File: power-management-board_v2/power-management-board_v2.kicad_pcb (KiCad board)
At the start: 2 copper layers, 90 x 70 mm, 130 parts, among them IC2 TLP7820_TP4,E, IC3 MCP2562, J1 Conn_01x02, J2 Conn_01x02, J3 Conn_01x04, J4 Conn_01x04, J5 Conn_01x04_Pin, J6 Conn_01x02_Pin, J7 Conn_01x02, J8 Conn_01x02, J9 Conn_01x02, Q3 SSM3K341R, Q4 SSM3K341R, SW1 SW_Push, SW3 SW_SPDT_312, U1 TLP293, U2 TPS54560BDDA, U3 STM32G431K8Tx, U4 NJM12888F33, U5 TLP293, U6 CZ3A07, U7 AP7375, U8 TLP293

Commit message: 完成
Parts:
- added D10: SS2040FL, 0Ikedalibrary:SOD-123FL, F.Cu at (42.1, 39.1)
- added D8: LED, LED_SMD:LED_0603_1608Metric_Pad1.05x0.95mm_HandSolder, F.Cu at (104.0, 24.3)
- added JP1: Jumper_2_Open, Connector_PinHeader_2.54mm:PinHeader_1x02_P2.54mm_Vertical, F.Cu at (33.7, 31.4)
- added K1: FBR562ND12-W, 0Ikedalibrary:FBR562ND12-W, F.Cu at (34.2, 53.7)
- added R34: 10k, Resistor_SMD:R_0603_1608Metric_Pad0.98x0.95mm_HandSolder, F.Cu at (37.5, 39.5)
- added R40: 10k, Resistor_SMD:R_0603_1608Metric_Pad0.98x0.95mm_HandSolder, B.Cu at (45.2, 34.5)
- added R41: 10k, Resistor_SMD:R_0603_1608Metric_Pad0.98x0.95mm_HandSolder, F.Cu at (101.5, 23.4)
- added U9: TLP293, Package_SO:SOIC-4_4.55x2.6mm_P1.27mm, B.Cu at (44.7, 39.6)
- C2, C27, D29, D30, Q3, Q4, R11, R12, R13, R14, R26, R30, R47: moved to B.Cu
- moved C29 148.3 mm to (100.5, 25.1)
- moved R2 141.3 mm to (94.2, 33.7), turned to -90 degrees
- moved R1 141.0 mm to (92.6, 26.3), turned to -90 degrees
- moved R7 139.2 mm to (96.4, 23.7), turned to 180 degrees
- moved C28 138.6 mm to (93.3, 36.2), turned to 180 degrees
- moved C26 137.8 mm to (92.6, 33.7), turned to -90 degrees
- moved R8 136.5 mm to (93.0, 23.7), turned to 180 degrees
- moved R29 135.9 mm to (92.6, 29.9), turned to 90 degrees
- moved R28 133.3 mm to (91.0, 31.7), turned to 90 degrees
- moved C30 130.5 mm to (101.1, 43.5), turned to -90 degrees
- moved C31 127.4 mm to (97.7, 43.5), turned to -90 degrees
- moved C25 125.9 mm to (93.9, 21.2), turned to 180 degrees
- moved C24 125.7 mm to (93.9, 17.8), turned to 180 degrees
- moved L1 122.3 mm to (99.4, 36.6), turned to -90 degrees
- moved D1 111.6 mm to (100.7, 29.1), turned to 90 degrees
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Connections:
- C2 pad 2: GND -> GNDPWR
- C27 pad 2: GND -> GNDPWR
- U3 pad 28: unconnected-(U3-PB5-Pad28) -> VCC_check
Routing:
- net +12VA: track 0.00 -> 69.7 mm, vias 0 -> 2
- net EN_return: track 0.00 -> 42.2 mm
- net stm32_EN_2: track 0.00 -> 40.2 mm, vias 0 -> 4
- net GND: track 21.4 -> 60.2 mm, vias 148 -> 86
- net stm32_EN_1: track 0.00 -> 38.7 mm, vias 0 -> 4
- net Net-(D29-A): track 0.00 -> 35.8 mm
- net VCC: track 0.00 -> 24.0 mm
- net Net-(K1B-N.C.): track 0.00 -> 22.7 mm
- net Net-(K1A-COM): track 0.00 -> 21.9 mm
- net +12V: track 15.6 -> 36.8 mm
- net VOUT: track 19.4 -> 0.00 mm, vias 87 -> 71
- net Net-(K1A-N.C.): track 0.00 -> 19.4 mm, vias 0 -> 1
- net INPUT_relay: track 8.15 -> 26.7 mm, vias 68 -> 55
- net VCC_check: track 0.00 -> 18.0 mm, vias 0 -> 1
- net Net-(D30-A): track 0.00 -> 17.1 mm
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- added copper zone on F.Cu, net +12V
- added copper zone on B.Cu, net GNDPWR
- added copper zone on F.Cu, net GNDPWR
- added copper zone on F.Cu, net Net-(D1-K)
- removed copper zone on B.Cu, net (none)
- removed copper zone on F.Cu, net (none)
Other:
- board text added: "12V"
- board text added: "12V OUT"
- board text added: "12V生成 入力"
- board text added: "EMS"
- board text removed: "2 1 G"
- board text removed: "EMS OUT"
- board text removed: "FAULT"
- board text removed: "IN1"
- board text removed: "IN2"
- board text removed: "i"
- board text removed: "s"
- board text removed: "逆接"

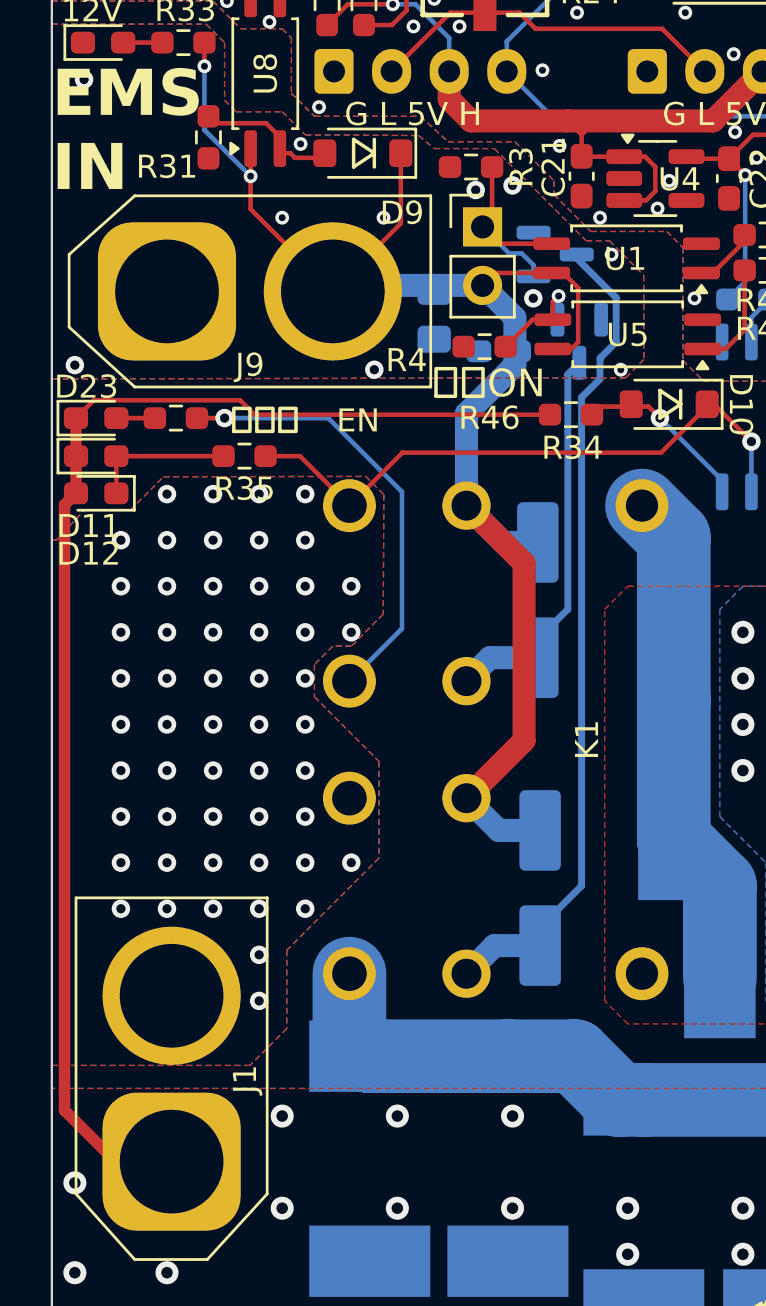
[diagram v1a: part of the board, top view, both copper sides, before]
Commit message: feat:ゲートに抵抗追加＆常時ON削除
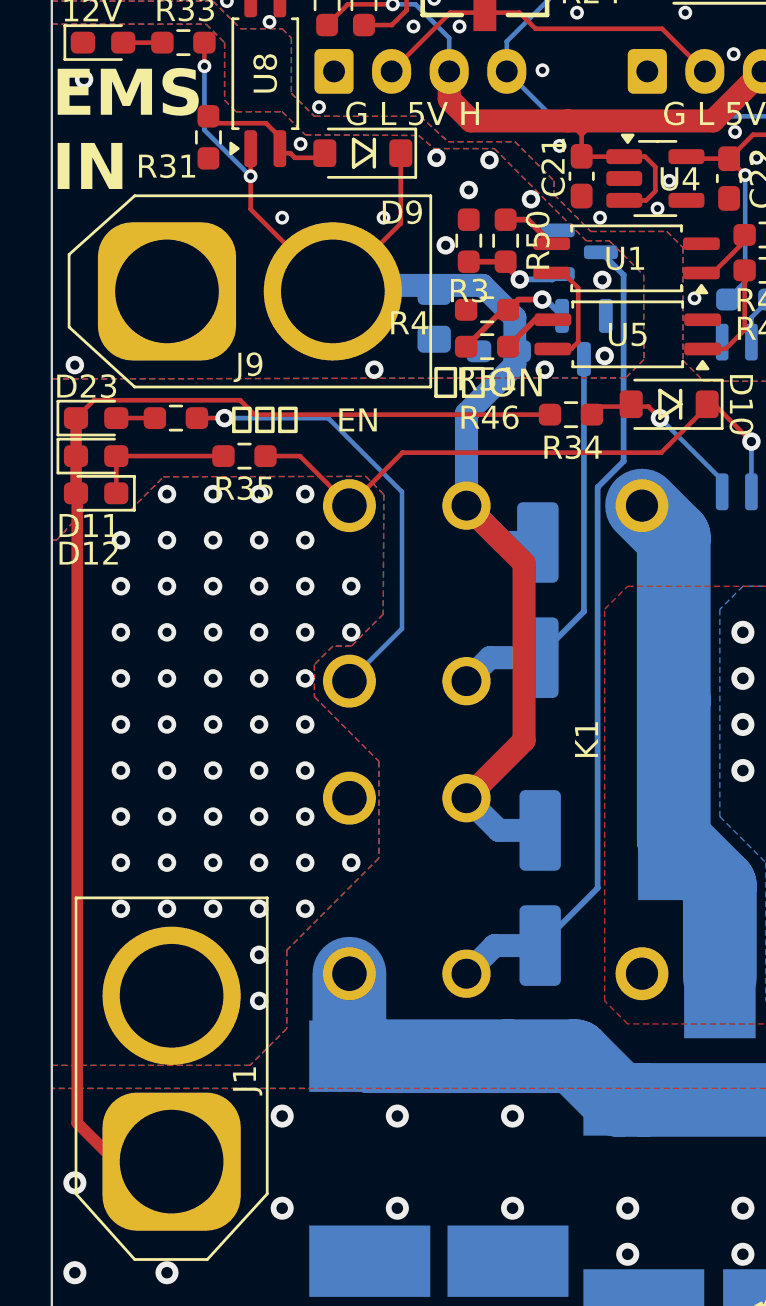
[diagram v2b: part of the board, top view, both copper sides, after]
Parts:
- removed JP1: Jumper_2_Open, Connector_PinHeader_2.54mm:PinHeader_1x02_P2.54mm_Vertical
- added R50: 470, Resistor_SMD:R_0603_1608Metric_Pad0.98x0.95mm_HandSolder, F.Cu at (34.7, 32.0)
- added R51: 470, Resistor_SMD:R_0603_1608Metric_Pad0.98x0.95mm_HandSolder, F.Cu at (33.9, 36.6)
- moved R3 3.20 mm to (33.1, 32.0), turned to 90 degrees
- moved R4 1.60 mm to (33.9, 35.0)
- moved Q3 1.05 mm to (37.9, 32.5)
- moved Q4 0.26 mm to (38.1, 36.2)
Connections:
- Q3 pad 1: GATE_A -> Net-(Q3-G)
- Q4 pad 1: GATE_B -> Net-(Q4-G)
- R3 pad 1: GATE_A -> Net-(Q3-G)
- R4 pad 1: GATE_B -> Net-(Q4-G)
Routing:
- net GATE_A: track 9.75 -> 2.43 mm
- net Net-(Q4-G): track 0.00 -> 5.30 mm, vias 0 -> 1
- net Net-(Q3-G): track 0.00 -> 4.37 mm, vias 0 -> 1
- net +12VA: track 69.7 -> 66.5 mm
- net GATE_B: track 4.71 -> 2.42 mm, vias 1 -> 0
- net GNDPWR: vias 11 -> 14

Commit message: シルク調整、DRC通した
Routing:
- net +12VA: track 66.5 -> 68.0 mm, vias 2 -> 3
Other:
- board text added: "VIN 逆接"
- board text added: "ソフトスタートOK"
- board text removed: "常時ON"
- board text removed: "駆動系"
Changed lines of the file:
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@@
 		(tags "resistor handsolder")
 		(property "Reference" "R46"
-			(at -13.6125 0 0)
+			(at -2.9125 1.95 0)
 			(layer "F.SilkS")
 			(effects
@@
 		(tags "resistor handsolder")
 		(property "Reference" "R3"
-			(at -2.2 0 0)
+			(at 2.05 0 0)
 			(layer "F.SilkS")
 			(effects
@@
 		(tags "resistor handsolder")
 		(property "Reference" "R50"
-			(at 0 -1.43 90)
+			(at -2.85 0 90)
 			(layer "F.SilkS")
 			(effects
@@
 		(tags "resistor handsolder")
 		(property "Reference" "R35"
-			(at 0 -1.43 0)
+			(at -3.0875 0 0)
 			(layer "F.SilkS")
 			(effects
@@
 		(tags "resistor handsolder")
 		(property "Reference" "R51"
-			(at 0 -1.43 0)
+			(at 0 -2.4 0)
 			(layer "F.SilkS")
 			(effects
@@
 		(tags "XT60 female vertical")
 		(property "Reference" "J9"
-			(at 3.6 3.2 180)
+			(at 5.35 3.55 180)
 			(layer "F.SilkS")
 			(effects
@@
 		(tags "resistor handsolder")
 		(property "Reference" "R4"
-			(at 3.3875 -0.6 0)
+			(at -0.05 -2.8 0)
 			(layer "F.SilkS")
 			(effects
@@
 		(tags "SOT TO_SOT_SMD")
 		(property "Reference" "Q4"
-			(at -2.3625 -0.8 180)
+			(at 0 -2.9 180)
 			(layer "B.SilkS")
 			(effects
@@
 		(tags "SOT TO_SOT_SMD")
 		(property "Reference" "Q3"
-			(at 1.85 -1.1 0)
+			(at 2.85 0 0)
 			(layer "B.SilkS")
 			(effects
@@
 		)
 	)
-	(gr_text "駆動系"
-		(at 22.75 40.4 0)
+	(gr_text "VIN\n逆接"
+		(at 18.65 43.7 0)
 		(layer "F.SilkS")
 		(effects
@@
 		)
 	)
-	(gr_text "5V 3.3V"
-		(at 25 16.6 0)
+	(gr_text "ソフトスタートOK"
+		(at 21.95 40.35 0)
 		(layer "F.SilkS")
 		(effects
@@
 		)
 	)
-	(gr_text "EN"
-		(at 27.35 40.4 0)
+	(gr_text "5V 3.3V"
+		(at 25 16.6 0)
 		(layer "F.SilkS")
 		(effects
@@
 		)
 	)
-	(gr_text "常時ON"
-		(at 31.5 38.9 0)
-		(layer "F.SilkS")
-		(effects
-			(font
-				(size 1.2 1.2)
-				(thickness 0.1524)
-			)
-			(justify left bottom)
-		)
-	)
 	(gr_text "EMS\nIN"
 		(at 15 30 0)
@@
 	)
 	(segment
+		(start 36.75 36.7)
+		(end 35.9 36.7)
+		(width 0.25)
+		(layer "F.Cu")
+		(net "+12VA")
+	)
+	(segment
 		(start 23.63 28)
 		(end 23.63 30.63)
@@
 	)
 	(via
+		(at 35.9 36.7)
+		(size 0.8)
+		(drill 0.4)
+		(layers "F.Cu" "B.Cu")
+		(net "+12VA")
+	)
+	(via
 		(at 23.63 29.2)
 		(size 0.6)
@@
 	)
 	(segment
+		(start 35.3625 36.7)
+		(end 35.2625 36.8)
+		(width 0.25)
+		(layer "B.Cu")
+		(net "+12VA")
+	)
+	(segment
 		(start 34.6 45.1)
 		(end 36.1 45.1)
@@
 	)
 	(segment
+		(start 35.9 36.7)
+		(end 35.3625 36.7)
+		(width 0.25)
+		(layer "B.Cu")
+		(net "+12VA")
+	)
+	(segment
 		(start 33.7 33.96)
 		(end 33.68 33.94)
@@
 	)
 	(segment
-		(start 34.7 31.0875)
-		(end 35.6575 31.0875)
+		(start 34.7 32.9125)
+		(end 34.7 33.067457)
 		(width 0.25)
 		(layer "F.Cu")
-		(net "GATE_A")
+		(net "Net-(Q3-G)")
 	)
 	(segment
-		(start 35.6575 31.0875)
-		(end 36.7 32.13)
+		(start 34.7 33.067457)
+		(end 35.314233 33.68169)
 		(width 0.25)
 		(layer "F.Cu")
-		(net "GATE_A")
+		(net "Net-(Q3-G)")
+	)
+	(segment
+		(start 34.7 32.9125)
+		(end 33.1 32.9125)
+		(width 0.25)
+		(layer "F.Cu")
+		(net "Net-(Q3-G)")
+	)
+	(via
+		(at 35.314233 33.68169)
+		(size 0.8)
+		(drill 0.4)
+		(layers "F.Cu" "B.Cu")
+		(net "Net-(Q3-G)")
+	)
+	(segment
+		(start 36.73081 33.68169)
+		(end 36.9625 33.45)
+		(width 0.25)
+		(layer "B.Cu")
+		(net "Net-(Q3-G)")
+	)
+	(segment
+		(start 35.314233 33.68169)
+		(end 36.73081 33.68169)
+		(width 0.25)
+		(layer "B.Cu")
+		(net "Net-(Q3-G)")
 	)
 	(via
@@
 	)
 	(segment
+		(start 34.7 31.0875)
+		(end 35.6575 31.0875)
+		(width 0.25)
+		(layer "F.Cu")
+		(net "GATE_A")
+	)
+	(segment
+		(start 35.6575 31.0875)
+		(end 36.7 32.13)
+		(width 0.25)
+		(layer "F.Cu")
+		(net "GATE_A")
+	)
+	(segment
 		(start 79.6 51.7125)
 		(end 79.6 50)
@@
 	)
 	(segment
+		(start 35.2575 34.555)
+		(end 36.291055 34.555)
+		(width 0.25)
+		(layer "F.Cu")
+		(net "Net-(Q4-G)")
+	)
+	(segment
+		(start 34.5875 35)
+		(end 32.9875 36.6)
+		(width 0.25)
+		(layer "F.Cu")
+		(net "Net-(Q4-G)")
+	)
+	(segment
+		(start 34.8125 35)
+		(end 34.5875 35)
+		(width 0.25)
+		(layer "F.Cu")
+		(net "Net-(Q4-G)")
+	)
+	(segment
+		(start 34.8125 35)
+		(end 35.2575 34.555)
+		(width 0.25)
+		(layer "F.Cu")
+		(net "Net-(Q4-G)")
+	)
+	(via
+		(at 36.291055 34.555)
+		(size 0.8)
+		(drill 0.4)
+		(layers "F.Cu" "B.Cu")
+		(net "Net-(Q4-G)")
+	)
+	(segment
+		(start 36.291055 34.555)
+		(end 36.4425 34.555)
+		(width 0.25)
+		(layer "B.Cu")
+		(net "Net-(Q4-G)")
+	)
+	(segment
+		(start 36.4425 34.555)
+		(end 37.15 35.2625)
+		(width 0.25)
+		(layer "B.Cu")
+		(net "Net-(Q4-G)")
+	)
+	(segment
 		(start 76 19.0675)
 		(end 76 20.6375)
@@
 		(net "Net-(U2-BOOT)")
 	)
-	(segment
-		(start 34.7 32.9125)
-		(end 34.7 33.067457)
-		(width 0.25)
-		(layer "F.Cu")
-		(net "Net-(Q3-G)")
-	)
-	(segment
-		(start 34.7 33.067457)
-		(end 35.314233 33.68169)
-		(width 0.25)
-		(layer "F.Cu")
-		(net "Net-(Q3-G)")
-	)
-	(segment
-		(start 34.7 32.9125)
-		(end 33.1 32.9125)
-		(width 0.25)
-		(layer "F.Cu")
-		(net "Net-(Q3-G)")
-	)
-	(via
-		(at 35.314233 33.68169)
-		(size 0.8)
-		(drill 0.4)
-		(layers "F.Cu" "B.Cu")
-		(net "Net-(Q3-G)")
-	)
-	(segment
-		(start 36.73081 33.68169)
-		(end 36.9625 33.45)
-		(width 0.25)
-		(layer "B.Cu")
-		(net "Net-(Q3-G)")
-	)
-	(segment
-		(start 35.314233 33.68169)
-		(end 36.73081 33.68169)
-		(width 0.25)
-		(layer "B.Cu")
-		(net "Net-(Q3-G)")
-	)
-	(segment
-		(start 35.2575 34.555)
-		(end 36.291055 34.555)
-		(width 0.25)
-		(layer "F.Cu")
-		(net "Net-(Q4-G)")
-	)
-	(segment
-		(start 34.5875 35)
-		(end 32.9875 36.6)
-		(width 0.25)
-		(layer "F.Cu")
-		(net "Net-(Q4-G)")
-	)
-	(segment
-		(start 34.8125 35)
-		(end 34.5875 35)
-		(width 0.25)
-		(layer "F.Cu")
-		(net "Net-(Q4-G)")
-	)
-	(segment
-		(start 34.8125 35)
-		(end 35.2575 34.555)
-		(width 0.25)
-		(layer "F.Cu")
-		(net "Net-(Q4-G)")
-	)
-	(via
-		(at 36.291055 34.555)
-		(size 0.8)
-		(drill 0.4)
-		(layers "F.Cu" "B.Cu")
-		(net "Net-(Q4-G)")
-	)
-	(segment
-		(start 36.291055 34.555)
-		(end 36.4425 34.555)
-		(width 0.25)
-		(layer "B.Cu")
-		(net "Net-(Q4-G)")
-	)
-	(segment
-		(start 36.4425 34.555)
-		(end 37.15 35.2625)
-		(width 0.25)
-		(layer "B.Cu")
-		(net "Net-(Q4-G)")
-	)
 	(zone
 		(net "IP")
@@
 	)
 	(group ""
-		(members "27c429ed-e494-4723-96aa-6c82fc9e4c01" "9c27f8ea-7dc1-4e73-aac6-d2837a3edbe1")
+		(members "9c27f8ea-7dc1-4e73-aac6-d2837a3edbe1")
 	)
 	(group ""
